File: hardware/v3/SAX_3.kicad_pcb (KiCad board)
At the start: 2 copper layers, 81 parts, among them J1 joystick, J2 LED 5 G D, J3 (G) SSD1306 SPI, J4 MIDI OUT Y:M5 - R:M4, J5 Batt, J6 Neck - Y:O BK:B R:3.3, J7 Conn_01x03_Female, J8 MXP5010, U1 74HC165, U2 74HC165, U3 74HC165, U4 Teensy3.2_breadboard_friendly

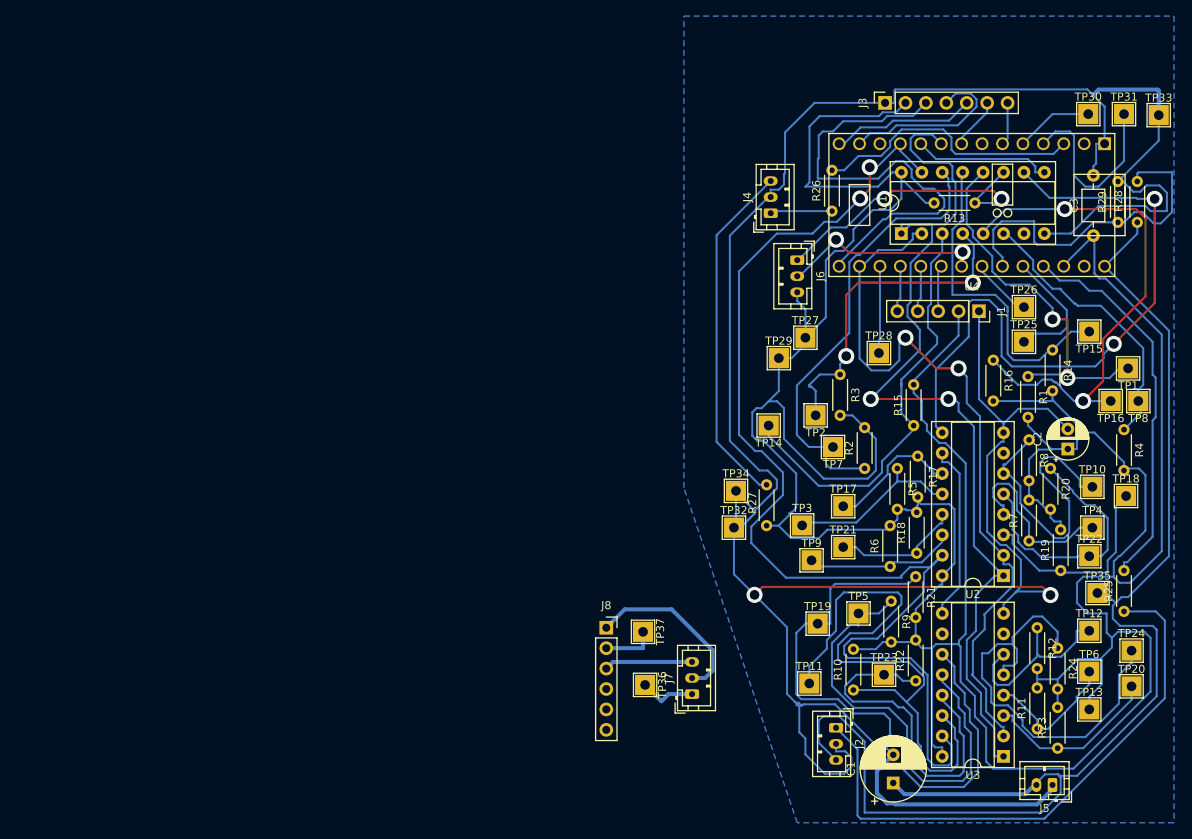
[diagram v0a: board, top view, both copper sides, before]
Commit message: Updated PCB with correct JST connectors, optimized PCB
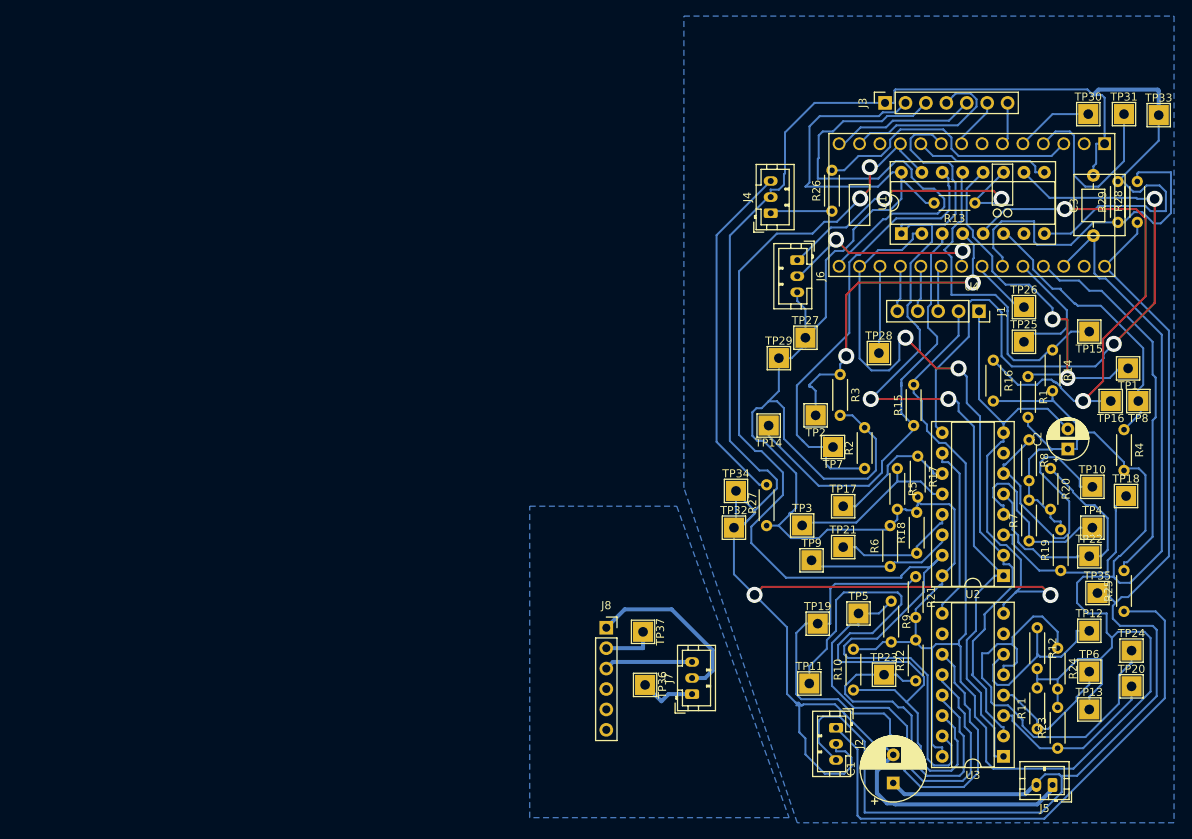
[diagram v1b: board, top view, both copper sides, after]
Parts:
- J2: value LED 5 G D -> LED strip
- J3: value (G) SSD1306 SPI -> SSD1306 SPI
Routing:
- net Net-(R14-Pad1): track 41.1 -> 42.2 mm
- added copper zone on B.Cu, net Net-(J8-Pad2)

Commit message: Updated pcb
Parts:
- moved J8 14.3 mm to (188.2, 106.7), turned to 180 degrees
- moved TP37 3.31 mm to (193.6, 95.6)
- moved TP36 2.34 mm to (192.9, 101.7)
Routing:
- net Net-(J8-Pad2): track 6.60 -> 20.8 mm
- net Net-(J7-Pad2): track 21.7 -> 15.0 mm
- net Net-(J7-Pad1): track 7.05 -> 5.29 mm
- net Net-(J7-Pad3): track 11.0 -> 12.7 mm
- net GND: track 355.2 -> 354.7 mm
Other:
- board text added: "TES sax v3 SPI SSD1306 LED strip"

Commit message: Updated PCB
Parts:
- added H1: MountingHole, MountingHole:MountingHole_4.3mm_M4_DIN965_Pad, F.Cu at (122.6, 66.4)
- added H2: MountingHole, MountingHole:MountingHole_4.3mm_M4_DIN965_Pad, F.Cu at (122.6, 89.4)
- added H3: MountingHole, MountingHole:MountingHole_3.2mm_M3_DIN965_Pad, F.Cu at (163.6, 75.5)
- added H4: MountingHole, MountingHole:MountingHole_3.2mm_M3_DIN965_Pad, F.Cu at (247.5, 21.4)
- added H5: MountingHole, MountingHole:MountingHole_3.2mm_M3_DIN965_Pad, F.Cu at (208.5, 21.4)
- J5: footprint Connector_JST:JST_PH_B2B-PH-K_1x02_P2.00mm_Vertical -> Connector_JST:JST_EH_B2B-EH-A_1x02_P2.50mm_Vertical
- moved J7 57.1 mm to (145.2, 78.4)
- moved J8 57.1 mm to (135.6, 84.3)
- moved TP36 57.1 mm to (140.3, 79.3)
- moved TP37 57.1 mm to (141.1, 73.3)
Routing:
- net +5V: track 162.7 -> 163.6 mm
